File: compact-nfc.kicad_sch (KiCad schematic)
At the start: 1 part, among them U1 ITR9702

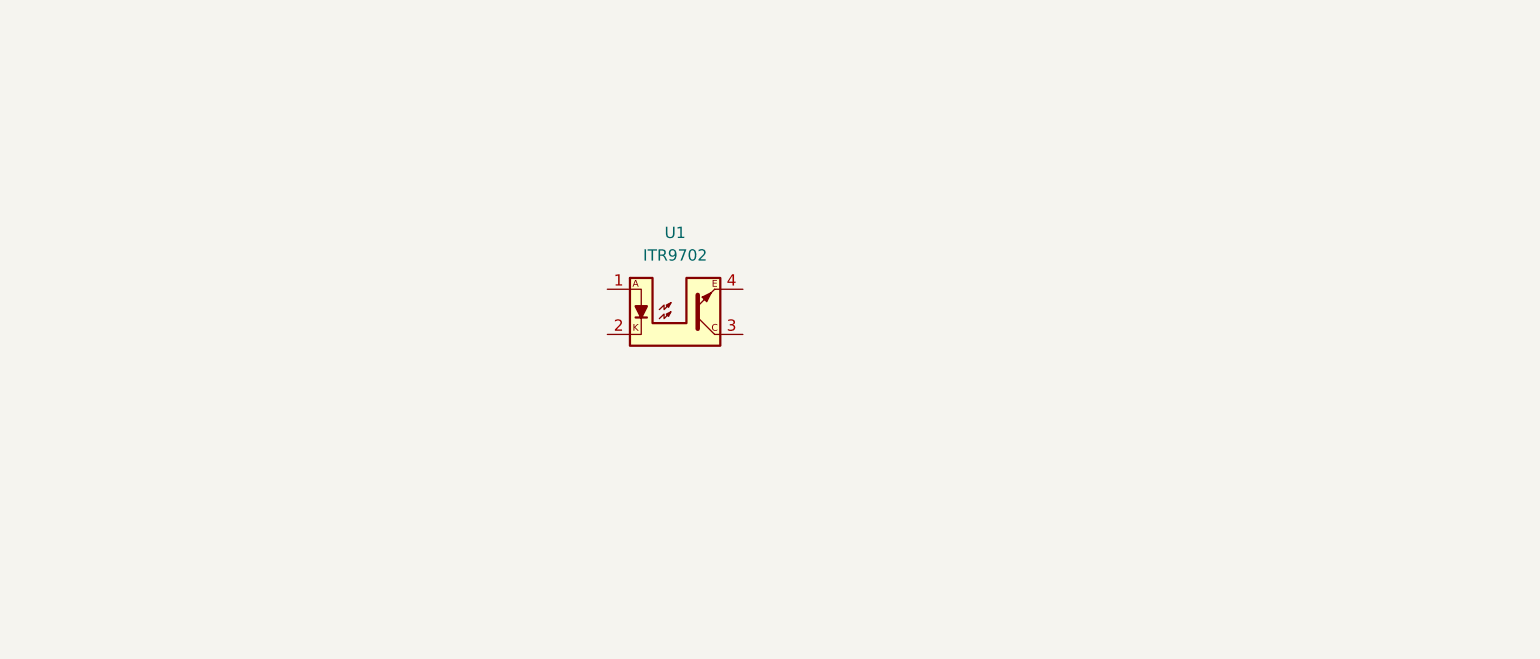
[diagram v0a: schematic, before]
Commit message: Add NFC chip and coil patterns for PCB
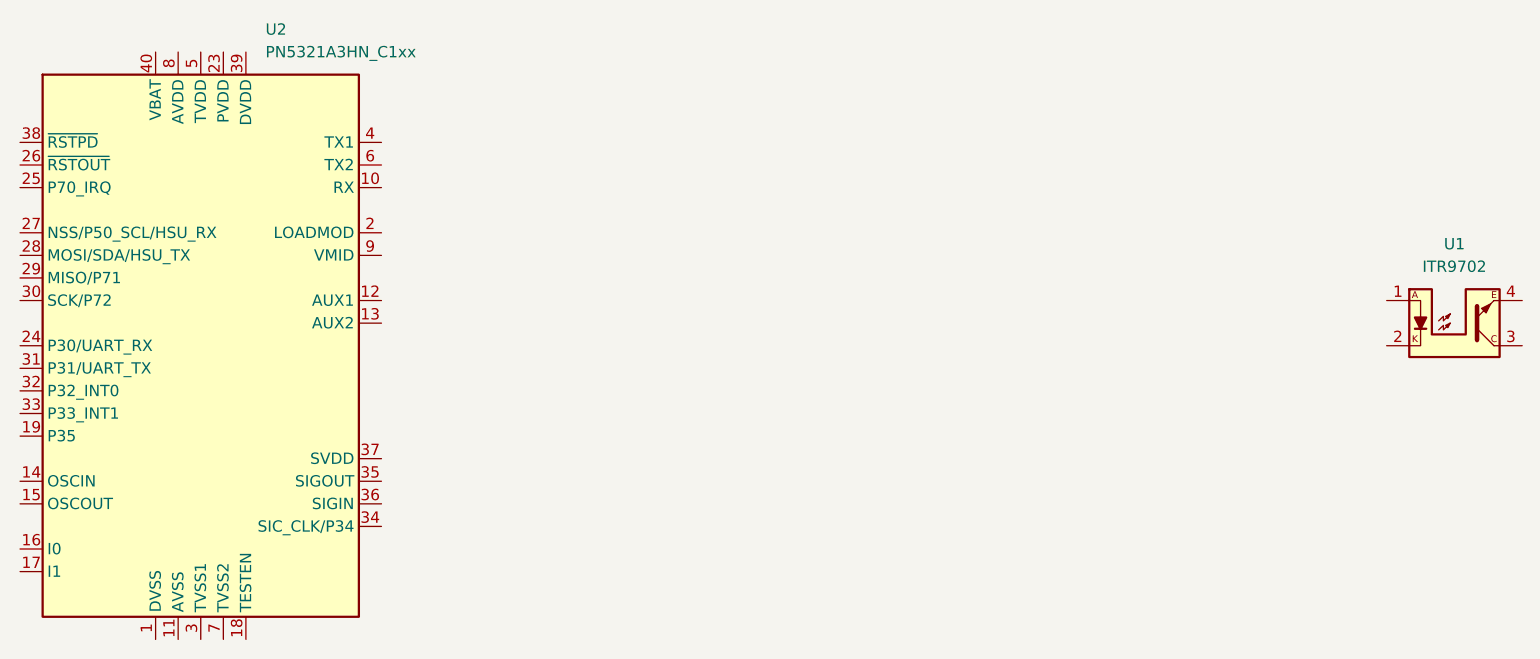
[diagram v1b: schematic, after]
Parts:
- added U2: PN5321A3HN_C1xx, Package_DFN_QFN:HVQFN-40-1EP_6x6mm_P0.5mm_EP4.1x4.1mm, symbol RF_NFC:PN5321A3HN_C1xx
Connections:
- new net: U2.11 (AVSS), U2.41 (AVSS)
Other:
- moved on the sheet: U1
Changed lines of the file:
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@@
 (kicad_sch (version 20230121) (generator eeschema)
   (paper "A4")
-  (symbol (lib_id "Sensor_Proximity_slot:ITR9702") (at 139.7 91.44 0) (unit 1)
+  (symbol (lib_id "RF_NFC:PN5321A3HN_C1xx") (at 86.36 95.25 0) (unit 1)
     (in_bom yes) (on_board yes) (dnp no) (fields_autoplaced)
-    (property "Reference" "U1" (at 139.7 82.55 0)
+    (property "Reference" "U2" (at 93.6341 59.69 0)
+      (effects (font (size 1.27 1.27)) (justify left))
+    )
+    (property "Value" "PN5321A3HN_C1xx" (at 93.6341 62.23 0)
+      (effects (font (size 1.27 1.27)) (justify left))
+    )
+    (property "Footprint" "Package_DFN_QFN:HVQFN-40-1EP_6x6mm_P0.5mm_EP4.1x4.1mm" (at 124.46 127 0)
+      (effects (font (size 1.27 1.27)) hide)
+    )
+    (property "Datasheet" "https://www.nxp.com/docs/en/nxp/data-sheets/PN532_C1.pdf" (at 86.36 90.17 0)
+      (effects (font (size 1.27 1.27)) hide)
+    )
+    (pin "40")
+    (pin "4")
+    (pin "15")
+    (pin "39")
+    (pin "11")
+    (pin "10")
+    (pin "1")
+    (pin "38")
+    (pin "20")
+    (pin "8")
+    (pin "16")
+    (pin "22")
+    (pin "13")
+    (pin "33")
+    (pin "32")
+    (pin "7")
+    (pin "35")
+    (pin "9")
+    (pin "34")
+    (pin "30")
+    (pin "24")
+    (pin "25")
+    (pin "31")
+    (pin "37")
+    (pin "17")
+    (pin "18")
+    (pin "36")
+    (pin "19")
+    (pin "2")
+    (pin "26")
+    (pin "21")
+    (pin "28")
+    (pin "23")
+    (pin "3")
+    (pin "29")
+    (pin "27")
+    (pin "41")
+    (pin "12")
+    (pin "14")
+    (pin "5")
+    (pin "6")
+    (instances
+      (project "compact-nfc"
+        (path "/21d4213f-f9dc-4f6d-96b5-1a03aba56c6c"
+          (reference "U2") (unit 1)
+        )
+      )
+    )
+  )
+  (symbol (lib_id "Sensor_Proximity_slot:ITR9702") (at 227.33 92.71 0) (unit 1)
+    (in_bom yes) (on_board yes) (dnp no) (fields_autoplaced)
+    (property "Reference" "U1" (at 227.33 83.82 0)
       (effects (font (size 1.27 1.27)))
     )
-    (property "Value" "ITR9702" (at 139.7 85.09 0)
+    (property "Value" "ITR9702" (at 227.33 86.36 0)
       (effects (font (size 1.27 1.27)))
     )
-    (property "Footprint" "OptoDevice_slot:Everlight_ITR9702" (at 139.7 97.79 0)
+    (property "Footprint" "OptoDevice_slot:Everlight_ITR9702" (at 227.33 99.06 0)
       (effects (font (size 1.27 1.27) italic) hide)
     )
-    (property "Datasheet" "https://www.everlighteurope.com/custom/files/datasheets/DRX-0000314.pdf" (at 138.43 85.09 0)
+    (property "Datasheet" "https://www.everlighteurope.com/custom/files/datasheets/DRX-0000314.pdf" (at 226.06 86.36 0)
       (effects (font (size 1.27 1.27)) hide)
     )

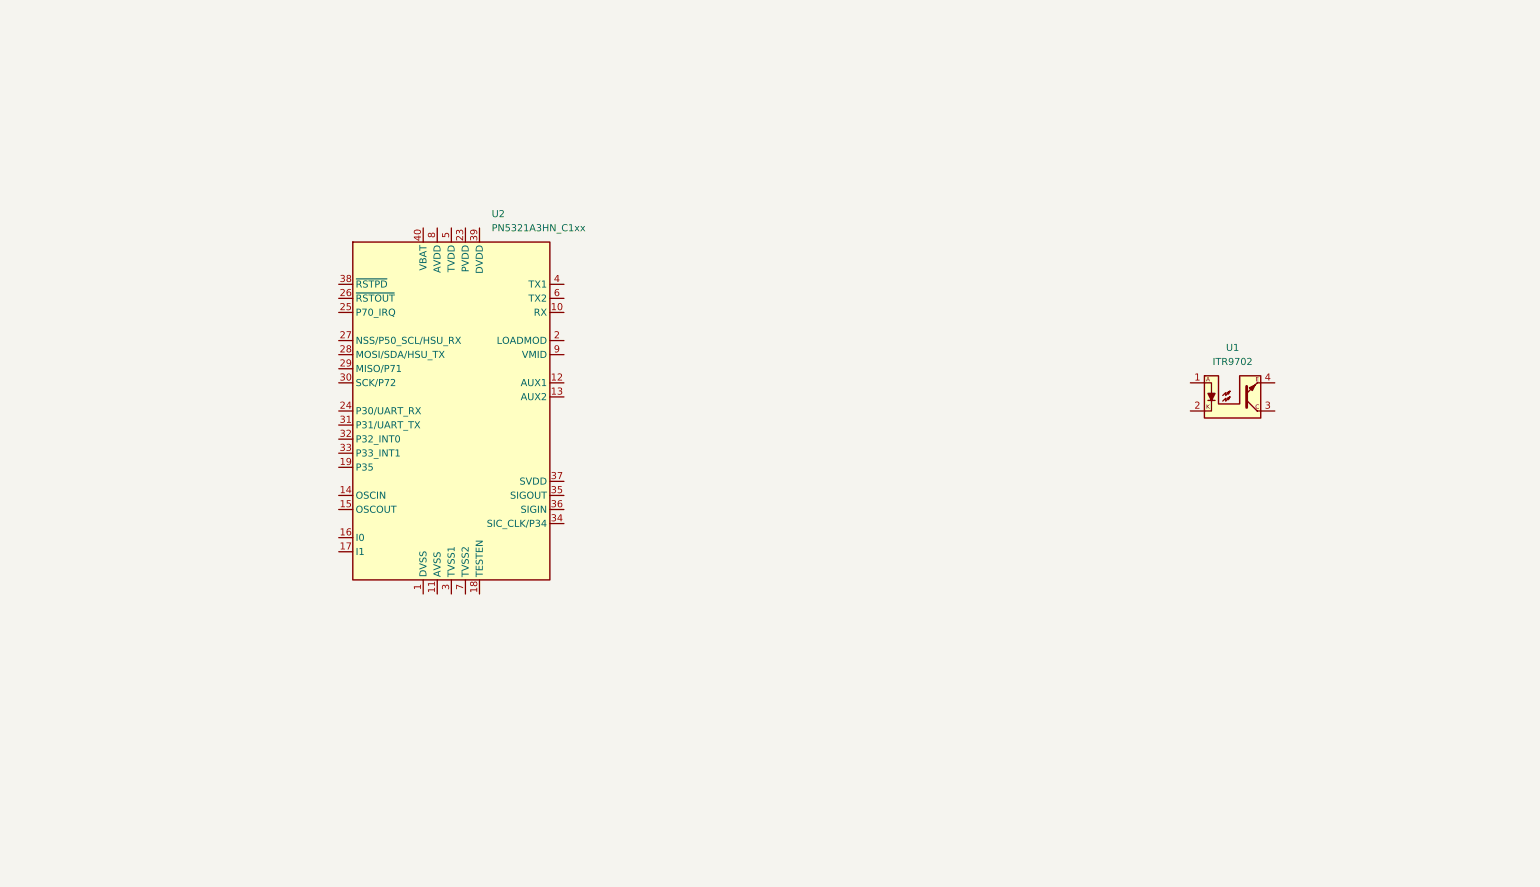
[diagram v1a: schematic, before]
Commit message: Add coupling components to NFC antenna
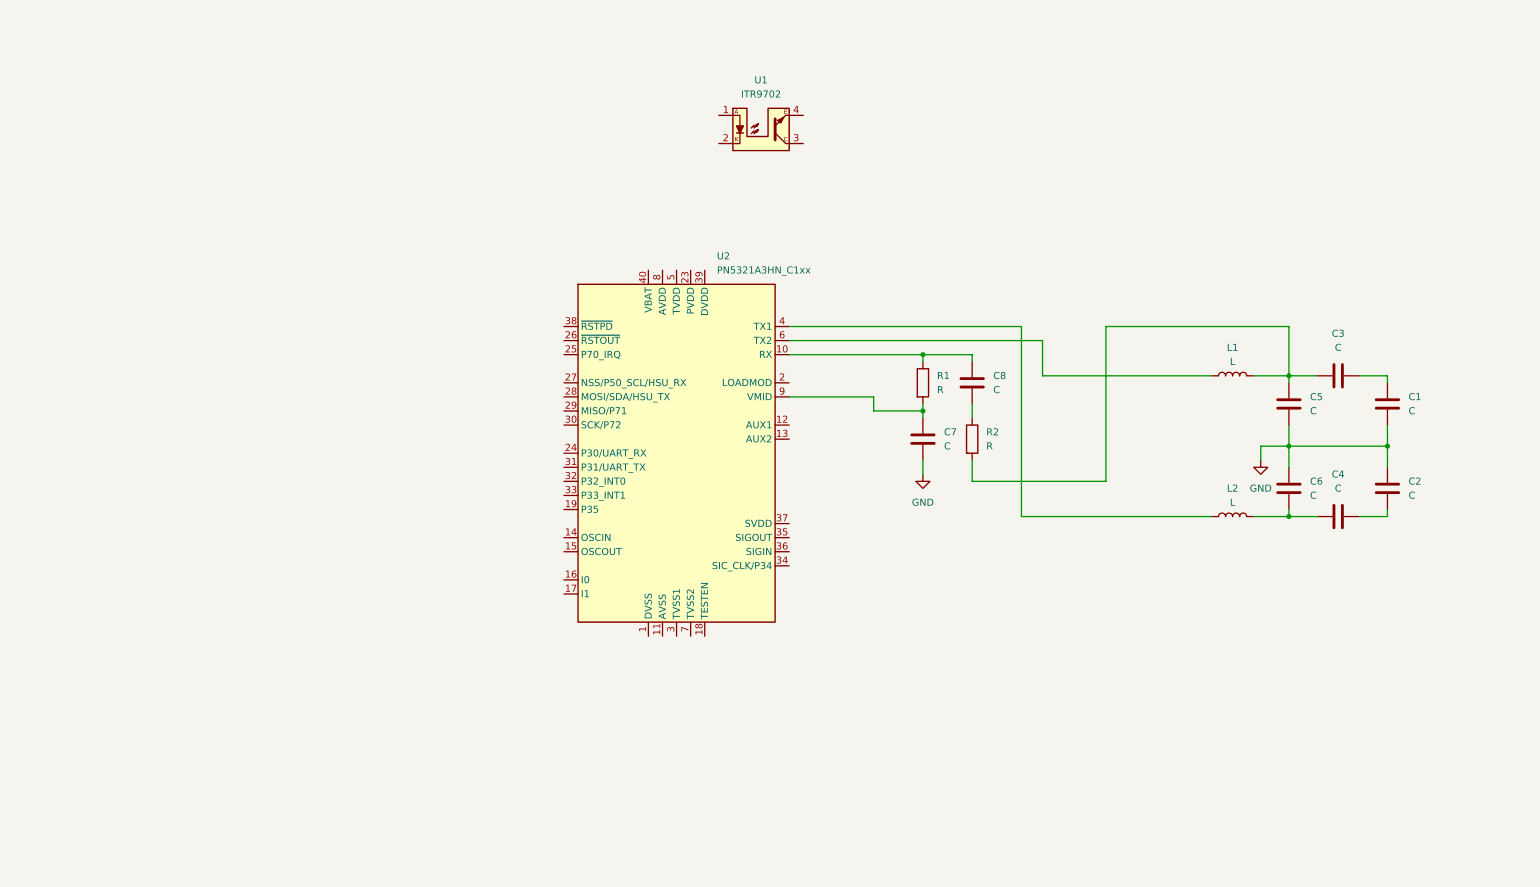
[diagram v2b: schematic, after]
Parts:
- added C1, C2, C3, C4, C5, C6, C7, C8: C, Capacitor_SMD:C_0805_2012Metric_Pad1.18x1.45mm_HandSolder, symbol Device:C
- added L1, L2: L, Inductor_SMD:L_1206_3216Metric_Pad1.22x1.90mm_HandSolder, symbol Device:L
- added R1, R2: R, Resistor_SMD:R_0805_2012Metric_Pad1.20x1.40mm_HandSolder, symbol Device:R
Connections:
- net at U2.10 (RX): now also C8.2, R1.1
- net at U2.4 (TX1): now also L2.1
- net at U2.6 (TX2): now also L1.1
- net at U2.9 (VMID): now also C7.2, R1.2
- new net: C2.2, C4.2
- new net: C3.1, C5.1, L1.2, R2.2
- new net: C8.1, R2.1
- new net: C1.1, C3.2
- new net: C4.1, C6.2, L2.2
- new net GND: C1.2, C2.1, C5.2, C6.1, C7.1
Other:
- moved on the sheet: U1, U2

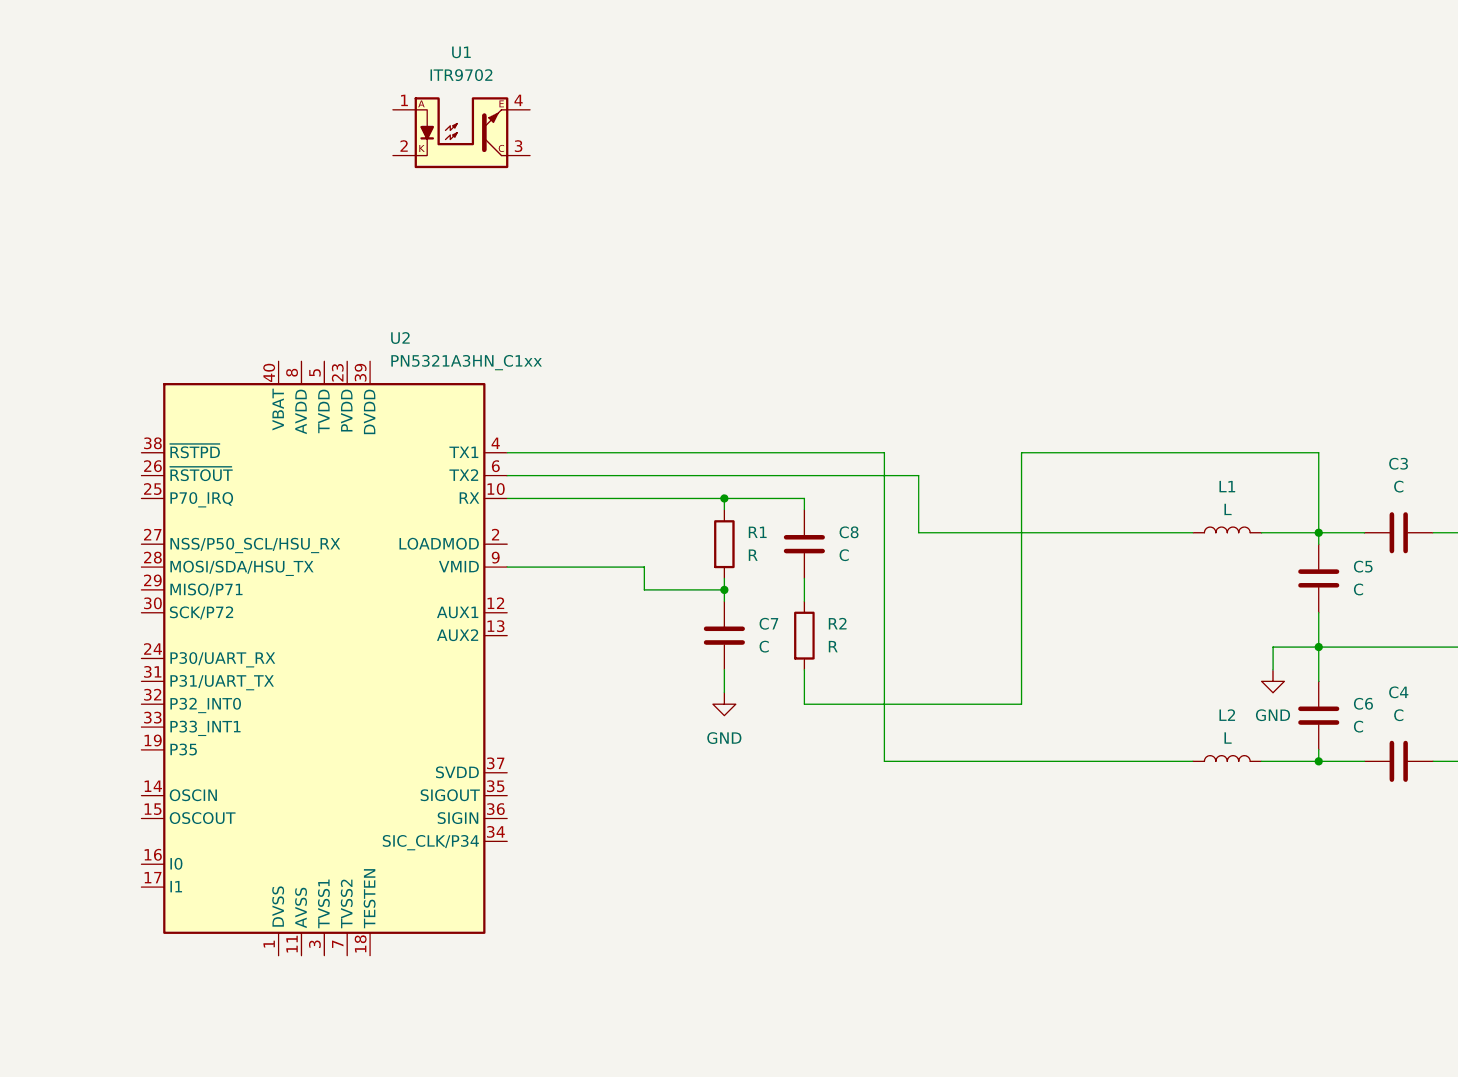
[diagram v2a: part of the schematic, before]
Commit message: Update optical sensor fixation pin
- Modify Everlight ITR9702 footprint (Everlight_ITR9702.kicad_mod)
- Update PCB layout and schematic accordingly
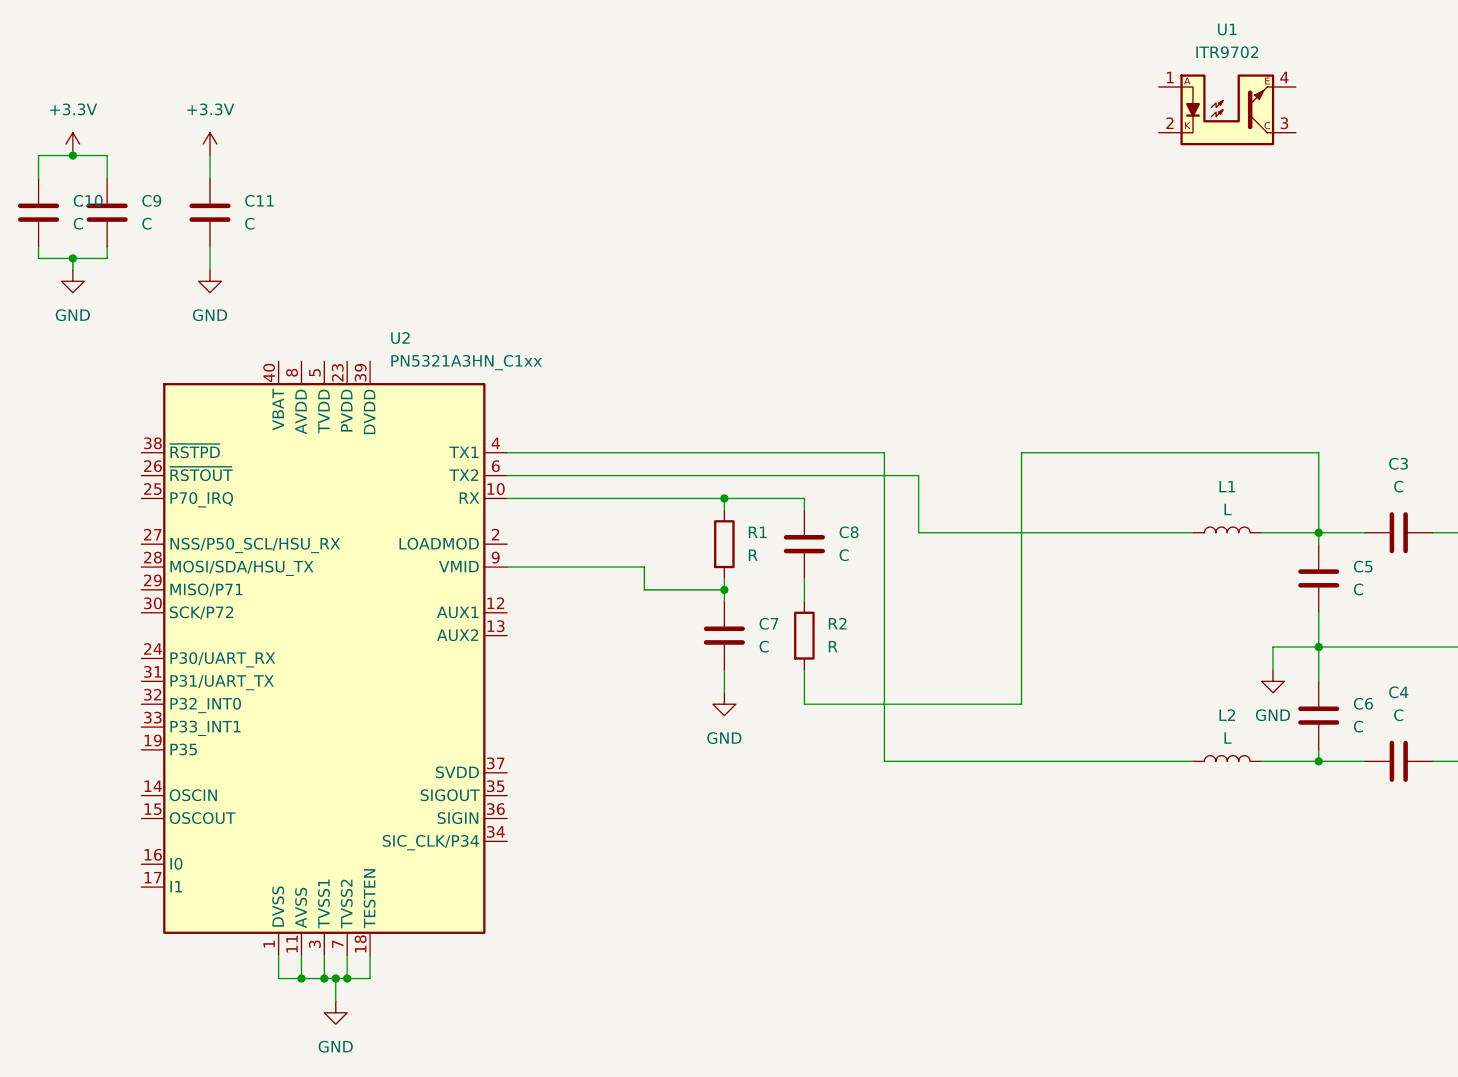
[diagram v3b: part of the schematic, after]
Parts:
- added C10, C11, C9: C, symbol Device:C
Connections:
- net GND: now also U2.1 (DVSS), U2.11 (AVSS), U2.18 (TESTEN), U2.3 (TVSS1), U2.41 (AVSS), U2.7 (TVSS2), C10.2, C11.2, C9.2
- new net +3.3V: C10.1, C11.1, C9.1
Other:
- moved on the sheet: U1
